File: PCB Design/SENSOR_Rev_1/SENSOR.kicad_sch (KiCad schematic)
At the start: 17 parts, among them J1 Conn_01x24_Pin, J2 Conn_01x24_Pin, U1 MS583730BA01-50, U2 LIS2HH12TR, U3 MMC5603NJ, U4 LSM6DSO32TR

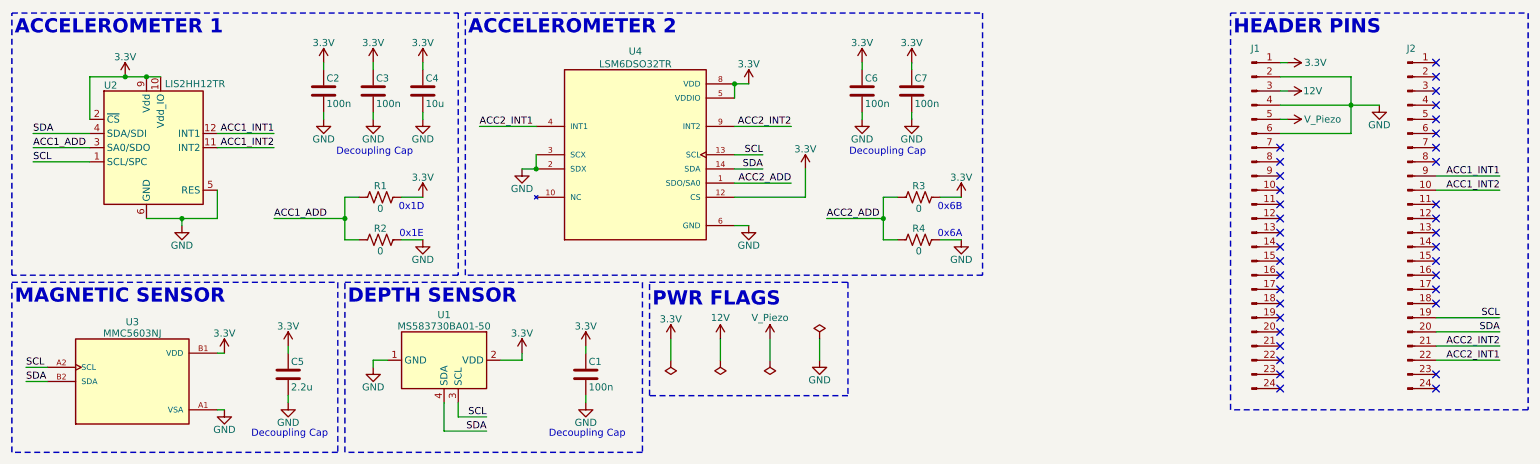
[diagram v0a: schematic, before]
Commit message: Updated Sensor to new Version
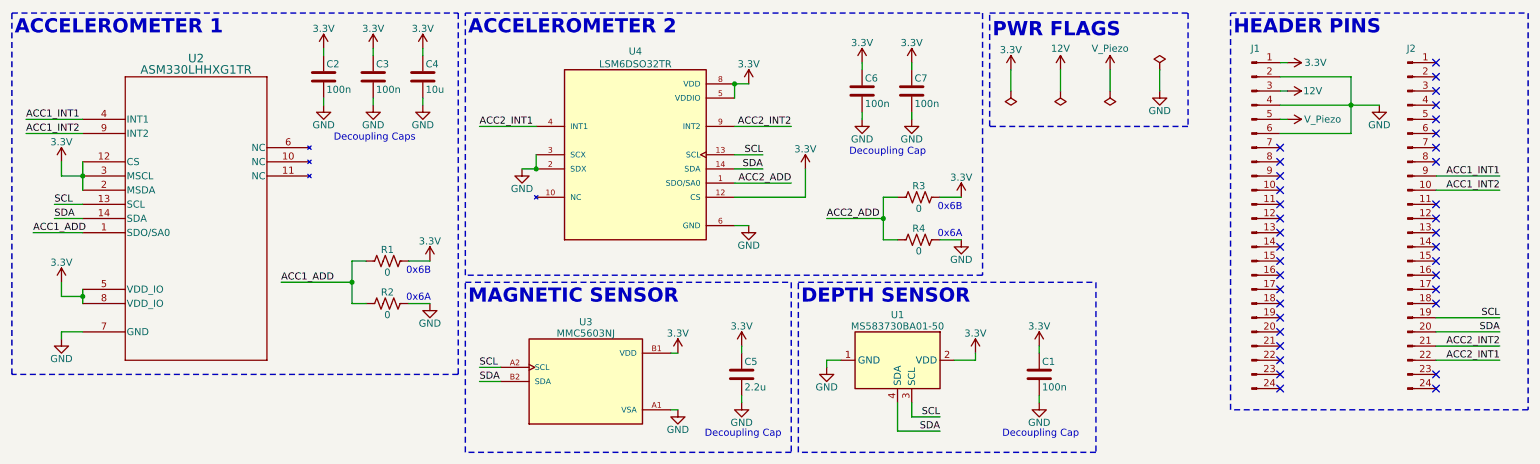
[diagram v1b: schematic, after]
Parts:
- removed U2: LIS2HH12TR, Package_LGA:LGA-12_2x2mm_P0.5mm, symbol Sensor_Motion:LIS2HH12
- added U2: ASM330LHHXG1TR, SENSOR:LGA14_2P5X3_STM, symbol SENSOR:ASM330LHHXG1TR
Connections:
- net 3.3V: now also U2.12 (CS), U2.2 (MSDA), U2.3 (MSCL), U2.5 (VDD_IO), U2.8 (VDD_IO)
- net ACC1_ADD: now also U2.1 (SDO/SA0)
- net ACC1_INT1: now also U2.4 (INT1)
- net ACC1_INT2: now also U2.9 (INT2)
- net GND: now also U2.7 (GND)
- net SCL: now also U2.13 (SCL)
- net SDA: now also U2.14 (SDA)
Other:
- note added: "Decoupling Caps"
- note removed: "0x1D"
- note removed: "0x1E"
- moved on the sheet: C1, C2, C3, C4, C5, R1, R2, U1, U3

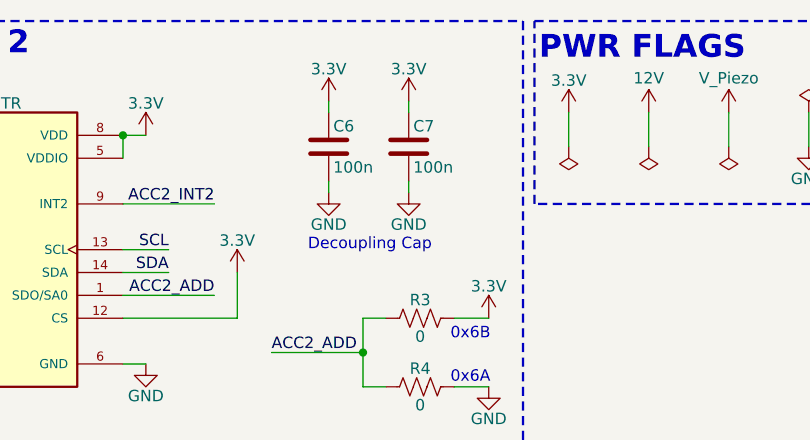
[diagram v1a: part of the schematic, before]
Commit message: Claude PCB Review
Made updates based on Claude's Review
- Added decoupling capacitor
- Verified CS pins
- Compared placement and connections to data sheets
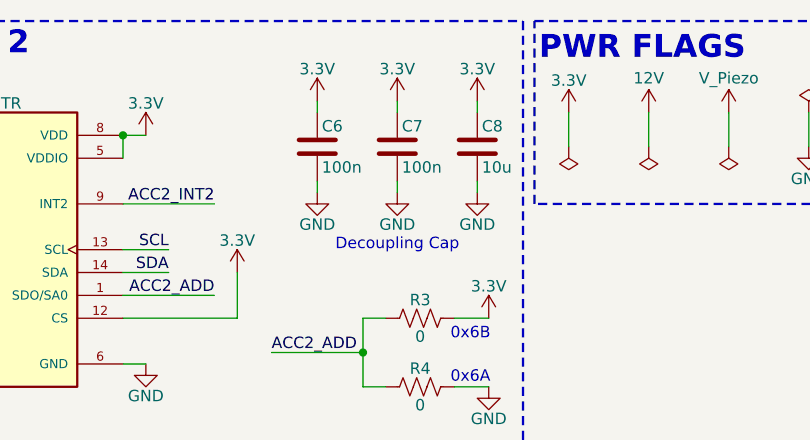
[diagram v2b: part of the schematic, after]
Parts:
- added C8: 10u, Capacitor_SMD:C_0603_1608Metric, symbol Device:C
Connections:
- net 3.3V: now also C8.1
- net GND: now also C8.2
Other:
- moved on the sheet: C6, C7

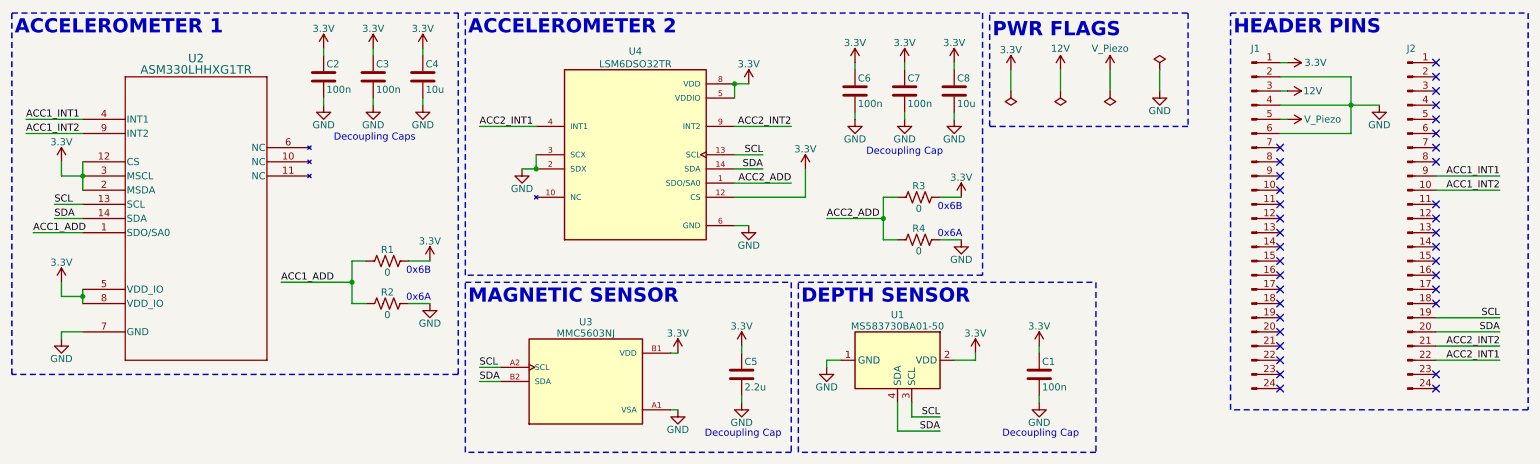
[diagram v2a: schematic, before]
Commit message: Claude Design Review
fix: tie ASM330 MSCL/MSDA to GND; DNP mark address jumpers R1/R3
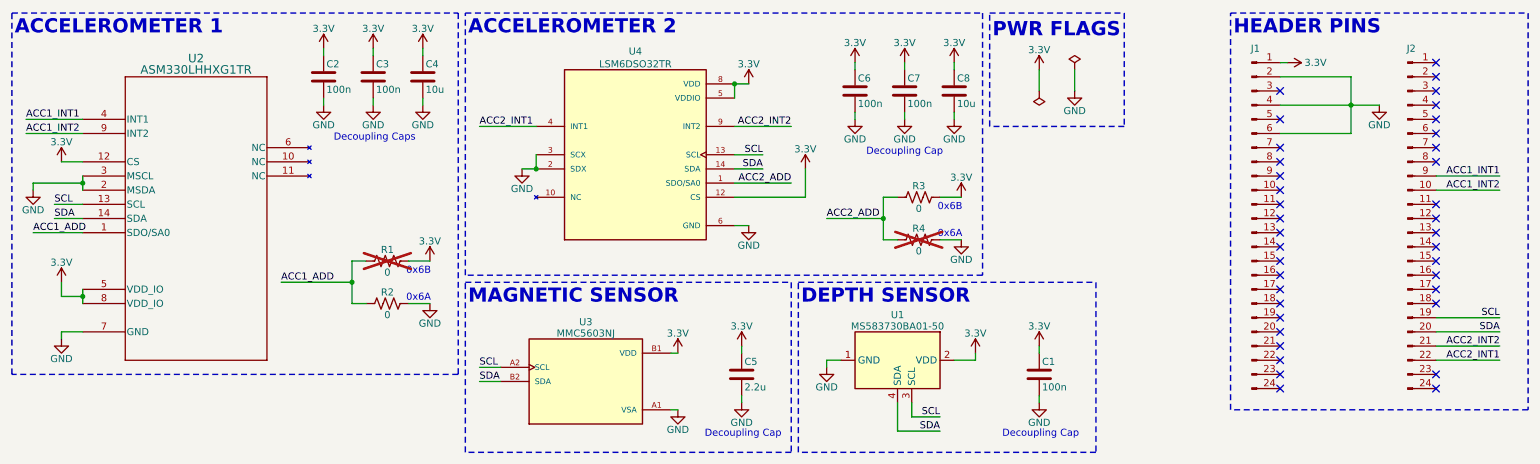
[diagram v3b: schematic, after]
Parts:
- R1, R4: now not fitted
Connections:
- net 3.3V: no longer U2.2 (MSDA), U2.3 (MSCL)
- net GND: now also U2.2 (MSDA), U2.3 (MSCL)
- net 12V: no longer names the net of J1.3 (Pin_3)
- net V_Piezo: no longer names the net of J1.5 (Pin_5)
- no-connect marks 36 -> 38

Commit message: SENSOR - Added and Exported 3D Model of PCB
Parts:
- U1: footprint Sensor_Pressure:TE_MS5837-xxBA -> SENSOR:TE_MS5837-xxBA
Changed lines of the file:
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@@
 			)
 		)
-		(property "Footprint" "Sensor_Pressure:TE_MS5837-xxBA"
+		(property "Footprint" "SENSOR:TE_MS5837-xxBA"
 			(at 171.45 74.93 0)
 			(effects
